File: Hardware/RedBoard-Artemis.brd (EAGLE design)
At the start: 68.6 x 53.3 mm, 114 parts, among them IC3 LM1117, J2 CORTEX_DEBUG, J3 POWER_JACKTOE, J5 USB-C, Q1 1.1A/60V/600mΩ, U1 ARTEMIS_MODULESMD, U3 AP2112-3.3V, U5 CH340C, Y1 32.768kHz

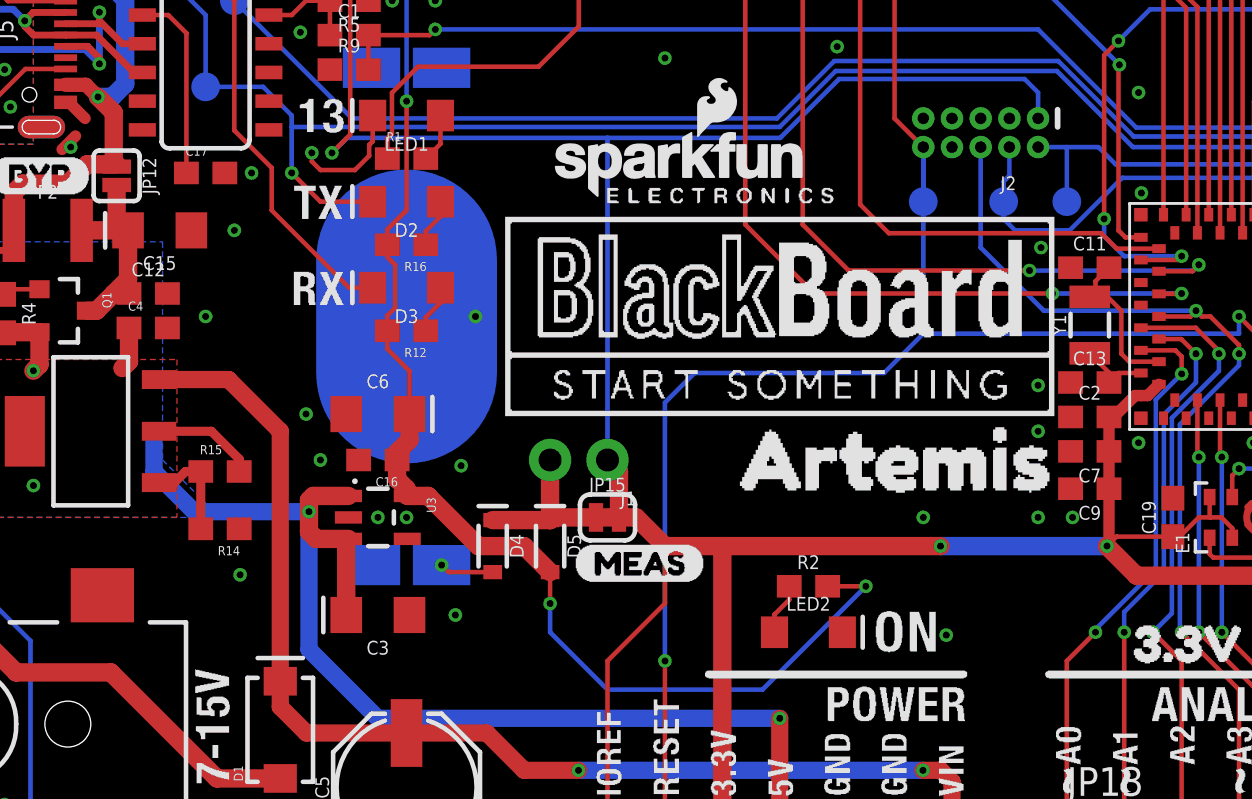
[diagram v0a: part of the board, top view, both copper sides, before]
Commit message: Move measurement PTH from under CR2032.
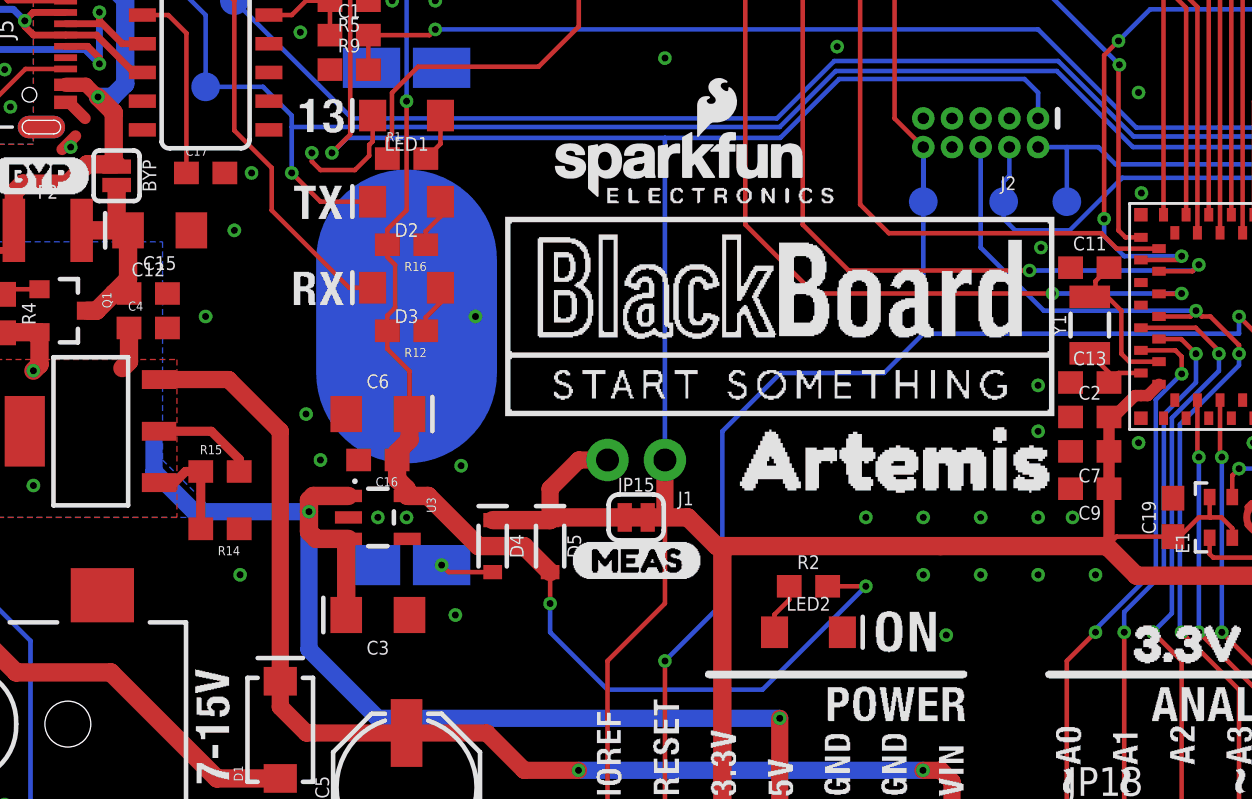
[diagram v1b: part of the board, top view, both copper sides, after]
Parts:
- moved J1 2.54 mm to (33.0, 20.3)
- moved JP15 1.27 mm to (31.8, 17.8)
- moved U$70 0.18 mm to (28.8, 15.9)
- renumbered JP12 to BYP
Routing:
- net N$3: track 7.28 -> 10.3 mm
- net !RESET: track 121.4 -> 119.1 mm
- net VDD: track 151.5 -> 151.3 mm, vias 3 -> 1
- net GND: vias 52 -> 58

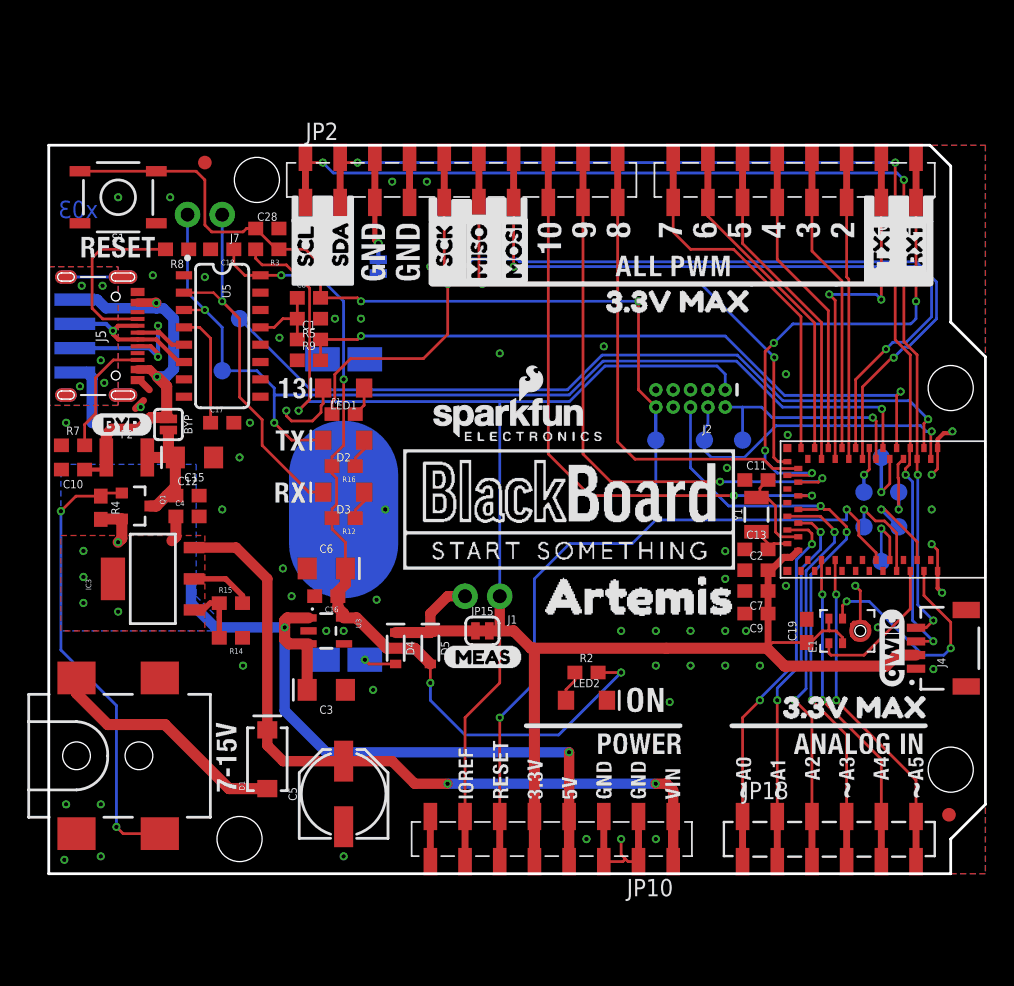
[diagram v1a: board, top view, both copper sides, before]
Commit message: Rename silk to RedBoard. Change version to v10.
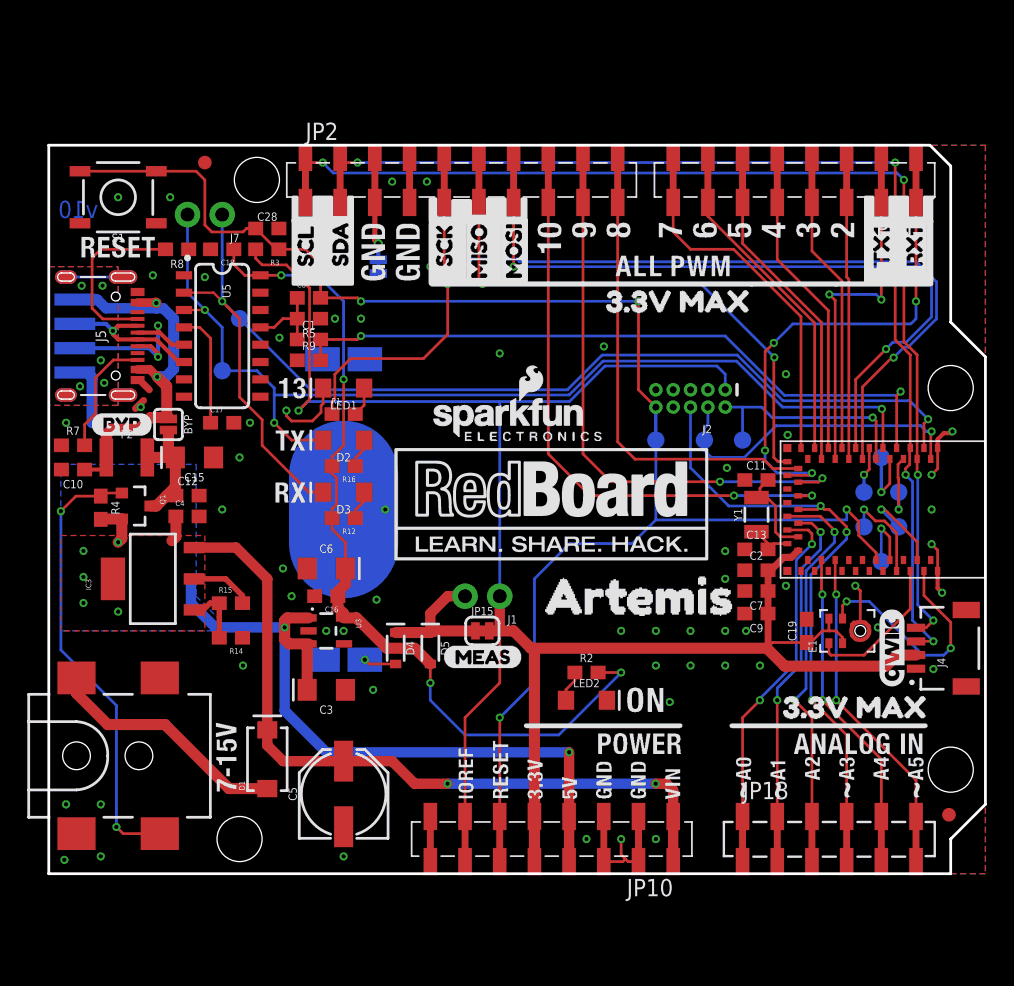
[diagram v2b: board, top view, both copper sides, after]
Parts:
- removed U$1, U$3: (no value), blackboardlogo:BLACKBOARDLOGO#PNG
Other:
- board text added: "v10"
- board text removed: "x03"

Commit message: Silk adjust
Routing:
- net N$10: track 7.60 -> 9.35 mm

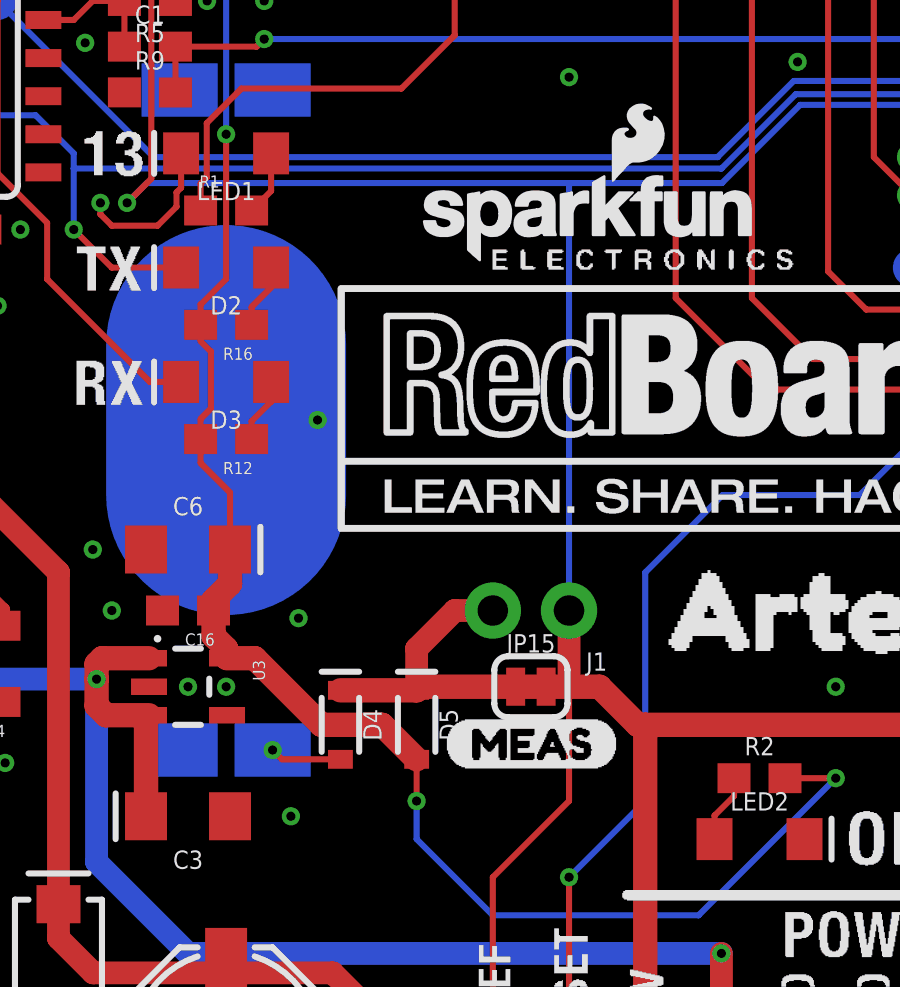
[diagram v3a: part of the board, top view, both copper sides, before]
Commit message: Remove diode from 3.3V rail. Move MEAS jumper.
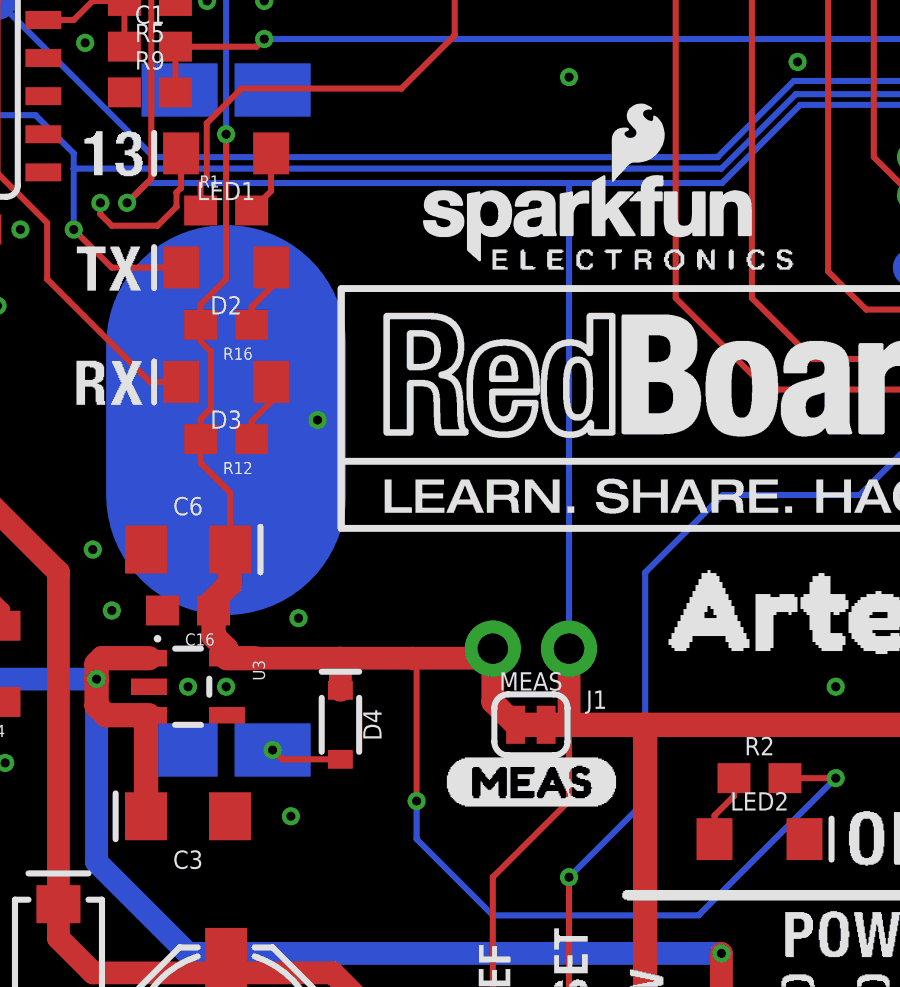
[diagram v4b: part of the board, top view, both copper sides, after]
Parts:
- removed D5: 1A/23V/620mV, SparkFun-DiscreteSemi:SOD-323
- removed JP15: (no value), SparkFun-Jumpers:SMT-JUMPER_2_NC_TRACE_SILK
- added MEAS: (no value), SparkFun-Jumpers:SMT-JUMPER_2_NC_TRACE_SILK
- D4: value 1A/23V/620mV -> 3A/10V/280mV
- moved J1 1.27 mm to (33.0, 19.1)
- moved U$70 1.27 mm to (28.8, 14.6)
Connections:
- removed net N$3: D4.C, D5.C, J1.2, JP15.1
- net 3.3V: now also D4.C, J1.2, MEAS.1; no longer D5.A
- net VDD: now also MEAS.2; no longer JP15.2
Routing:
- net N$3: track 10.3 -> 0.00 mm
- net 3.3V: track 63.9 -> 73.3 mm
- net VDD: track 151.3 -> 150.7 mm

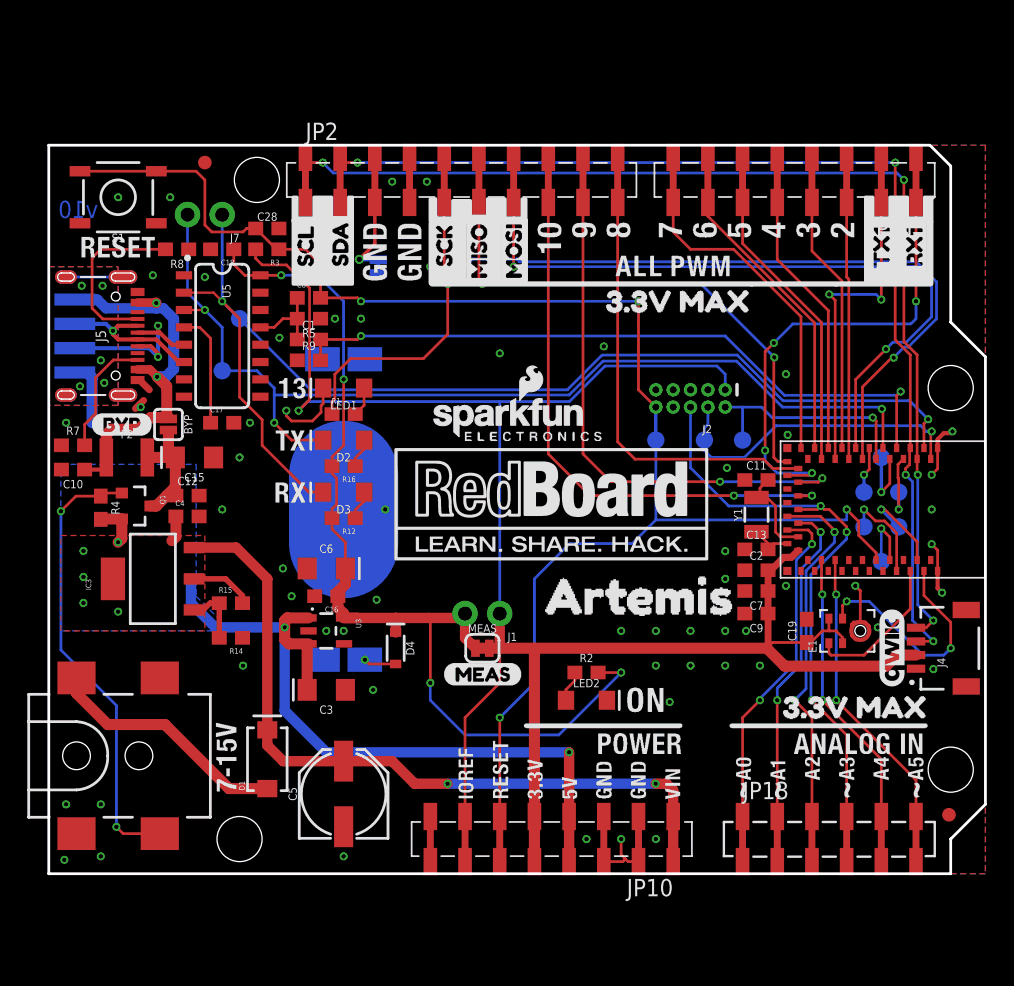
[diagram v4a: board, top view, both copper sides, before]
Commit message: Add PTH connectors to edges of board.
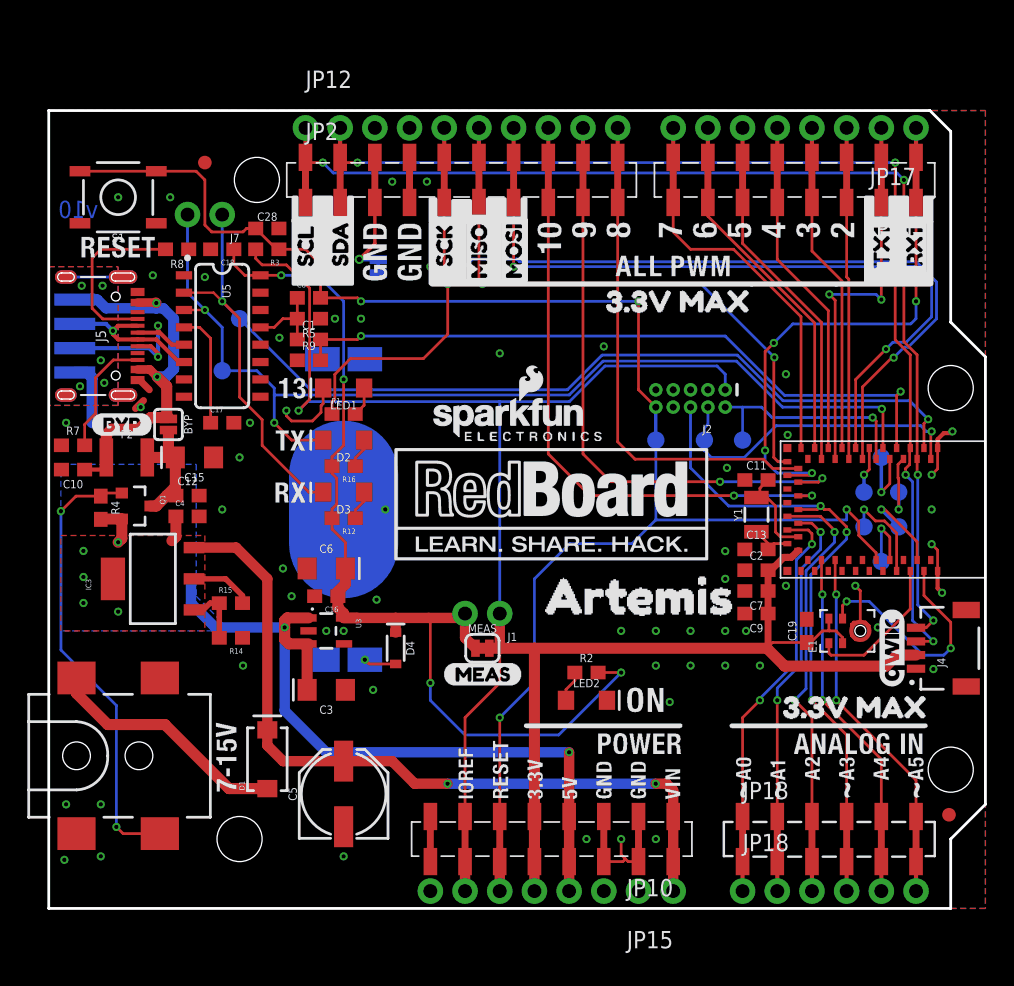
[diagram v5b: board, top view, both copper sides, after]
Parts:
- added JP12: M10NO_SILK, SparkFun-Connectors:1X10_NO_SILK
- added JP15: (no value), SparkFun-Connectors:1X08_NO_SILK
- added JP17: JP11, SparkFun-Connectors:1X08_NO_SILK
- added JP18: (no value), SparkFun-Connectors:1X06_NO_SILK@1
- Q1: value 1.1A/60V/600mΩ -> 2.5A/30V/105mΩ
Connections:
- net !RESET: now also JP15.6
- net 5V: now also JP15.4
- net D14/SDA: now also JP12.2
- net D18/A2: now also JP18.3
- net D20/A4: now also JP18.5
- net GND: now also JP12.3, JP12.4, JP15.2, JP15.3
- net VDD: now also JP15.5, JP15.7
- net VIN: now also JP15.1
- net ~D0/RXI-1: now also JP17.1
- net ~D1/TXO-1: now also JP17.2
- net ~D10/A10: now also JP12.8
- net ~D11/MOSI: now also JP12.7
- net ~D12/MISO: now also JP12.6
- net ~D13/SCK: now also JP12.5
- net ~D15/SCL: now also JP12.1
- net ~D16/A0: now also JP18.1
- net ~D17/A1: now also JP18.2
- net ~D19/A3: now also JP18.4
- net ~D2/A6: now also JP17.3
- net ~D21/A5: now also JP18.6
- net ~D3: now also JP17.4
- net ~D4: now also JP17.5
- net ~D5: now also JP17.6
- net ~D6: now also JP17.7
- net ~D7: now also JP17.8
- net ~D8/A8: now also JP12.10
- net ~D9/A9: now also JP12.9
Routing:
- net VDD: track 150.7 -> 155.1 mm
- net ~D19/A3: track 46.1 -> 48.3 mm
- net VIN: track 54.8 -> 57.0 mm
- net 5V: track 63.6 -> 65.7 mm
- net ~D21/A5: track 24.5 -> 26.7 mm
- net ~D17/A1: track 27.3 -> 29.5 mm
- net ~D16/A0: track 28.0 -> 30.2 mm
- net D20/A4: track 23.9 -> 26.1 mm
- net D18/A2: track 29.9 -> 32.0 mm
- net ~D9/A9: track 42.1 -> 44.2 mm
- net ~D8/A8: track 34.9 -> 37.0 mm
- net ~D7: track 27.0 -> 29.2 mm
- net ~D6: track 24.5 -> 26.7 mm
- net ~D5: track 24.5 -> 26.6 mm
- net ~D4: track 22.8 -> 25.0 mm
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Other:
- board size 68.6 x 53.3 mm -> 68.6 x 58.4 mm
